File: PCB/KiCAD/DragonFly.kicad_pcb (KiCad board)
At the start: 2 copper layers, 120 x 93 mm, 136 parts, among them CON1 AVR-ISP-6, J1 USB_OTG, J2 JACK_TRS_3pins, J3 MIC, J7 Conn_Coaxial, K1 TQ2-12VDC, P4 CONN_01X01, P5 CONN_01X01, P6 CONN_01X01, P7 CONN_01X01, Q1 MMBFJ310LT1G, Q10 MMBT4401LT1G, Q11 BFG591, Q12 IRF610, Q2 MMBT2222A, Q3 SI2301-TP, Q4 SI2301-TP, Q5 MMBT2222A, Q6 MMBFJ310LT1G, T1 1_9, T2 1_4, T3 1_4, U1 ADE-1, U10 LD1117S33TR, U2 ATMEGA8-16AU, U3 ADuM1201CR, U4 LM78L06, U5 SA612, U6 FT232RL, U7 SI5351, U8 LM78L06, U9 SA612, Y1 8Mhz, Y2 8Mhz, Y3 8Mhz, Y4 8Mhz, Y5 8Mhz, Y6 8Mhz, Y7 8Mhz, Y8 27Mhz

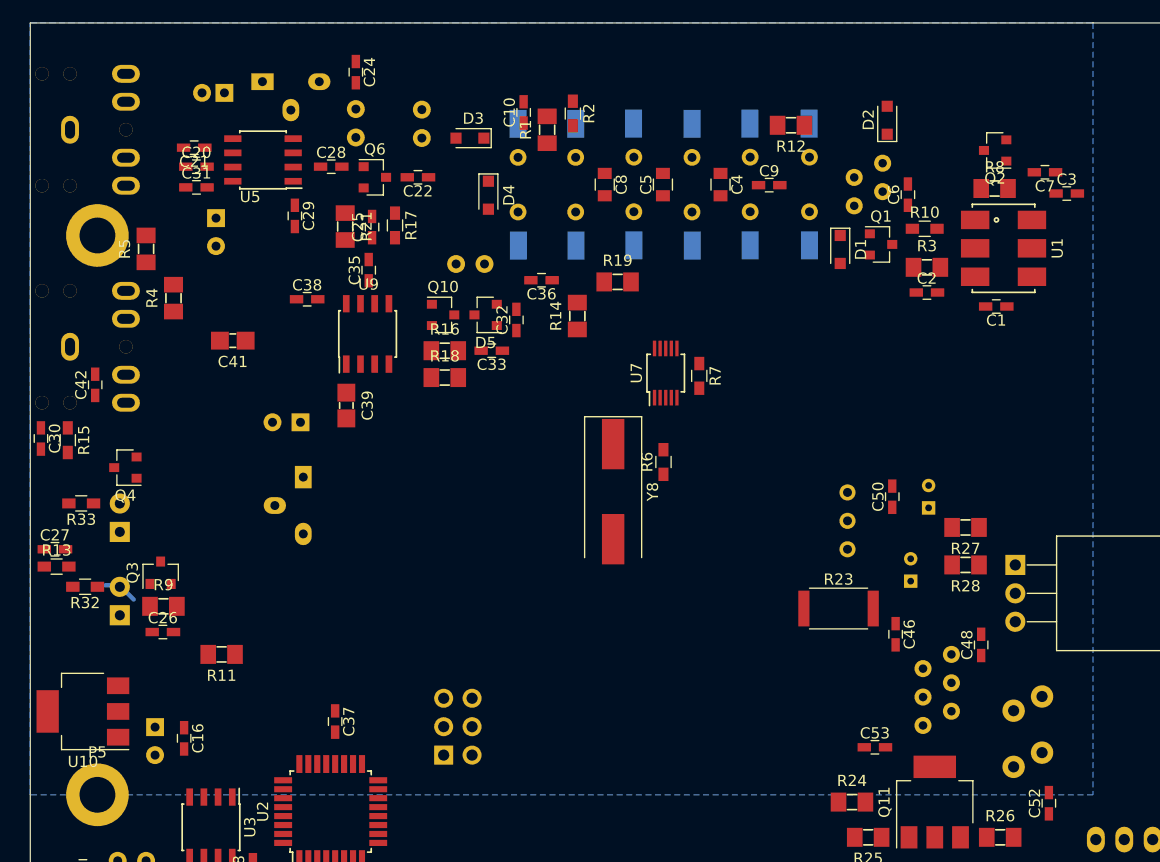
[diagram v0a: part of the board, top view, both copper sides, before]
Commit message: diode mixer on discrete components, begin move to DragonFly libs
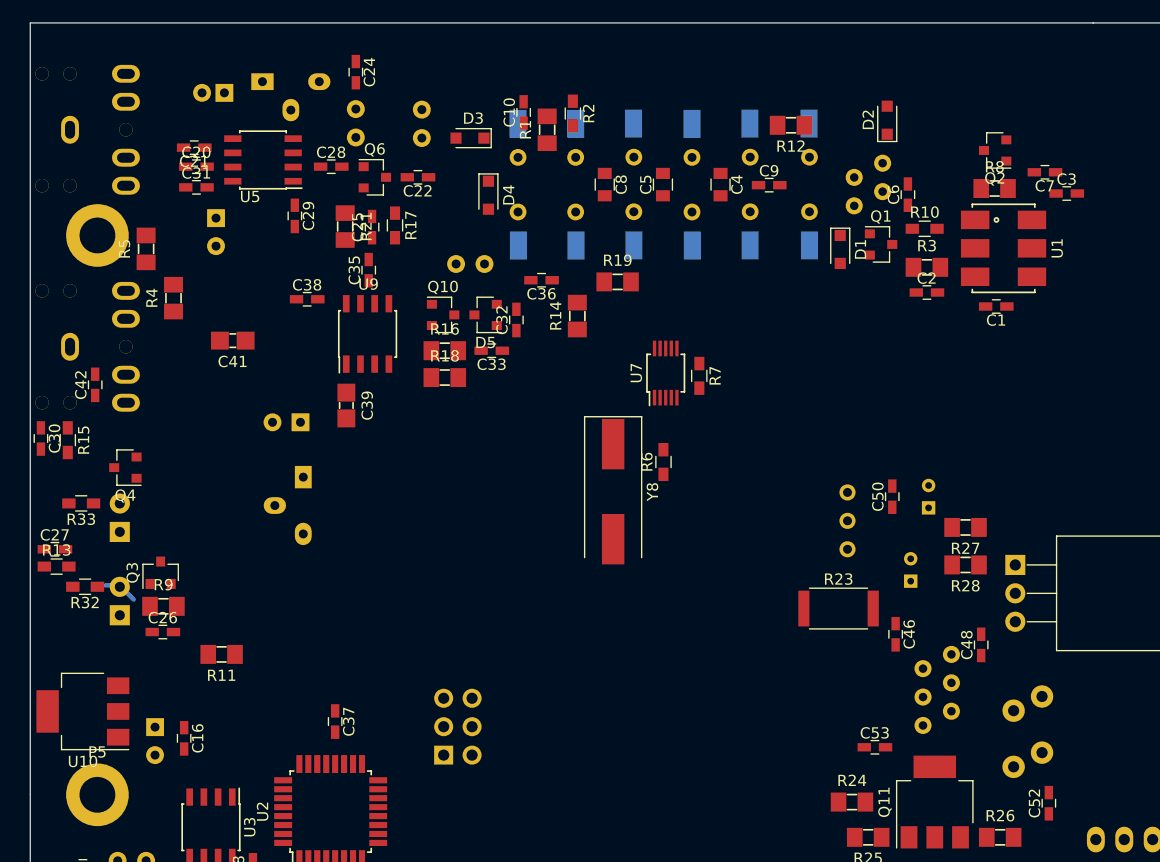
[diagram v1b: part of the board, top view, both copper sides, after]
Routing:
- removed copper zone on B.Cu, net GND
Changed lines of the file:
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@@
     (links 287)
     (no_connects 268)
-    (area 34.949999 19.949999 155.050001 113.050001)
+    (area 31.095 19.949999 157.085 176.075)
     (thickness 1.6)
     (drawings 6)
@@
   (layers
     (0 F.Cu signal)
-    (31 B.Cu signal hide)
+    (31 B.Cu signal)
     (32 B.Adhes user)
     (33 F.Adhes user)
@@
   (segment (start 41.7 70.27) (end 42.97 70.27) (width 0.4) (layer B.Cu) (net 88) (status 10))
   (segment (start 42.97 70.27) (end 44.24 71.54) (width 0.4) (layer B.Cu) (net 88) (status 20))
-  (zone (net 1) (net_name GND) (layer B.Cu) (hatch edge 0.508)
-    (connect_pads (clearance 0.2))
-    (min_thickness 0.2)
-    (fill yes (arc_segments 16) (thermal_gap 0.22) (thermal_bridge_width 0.501))
-    (polygon
-      (pts
-        (xy 130 89) (xy 35 89) (xy 35 20) (xy 130 20)
-      )
-    )
-  )
 )

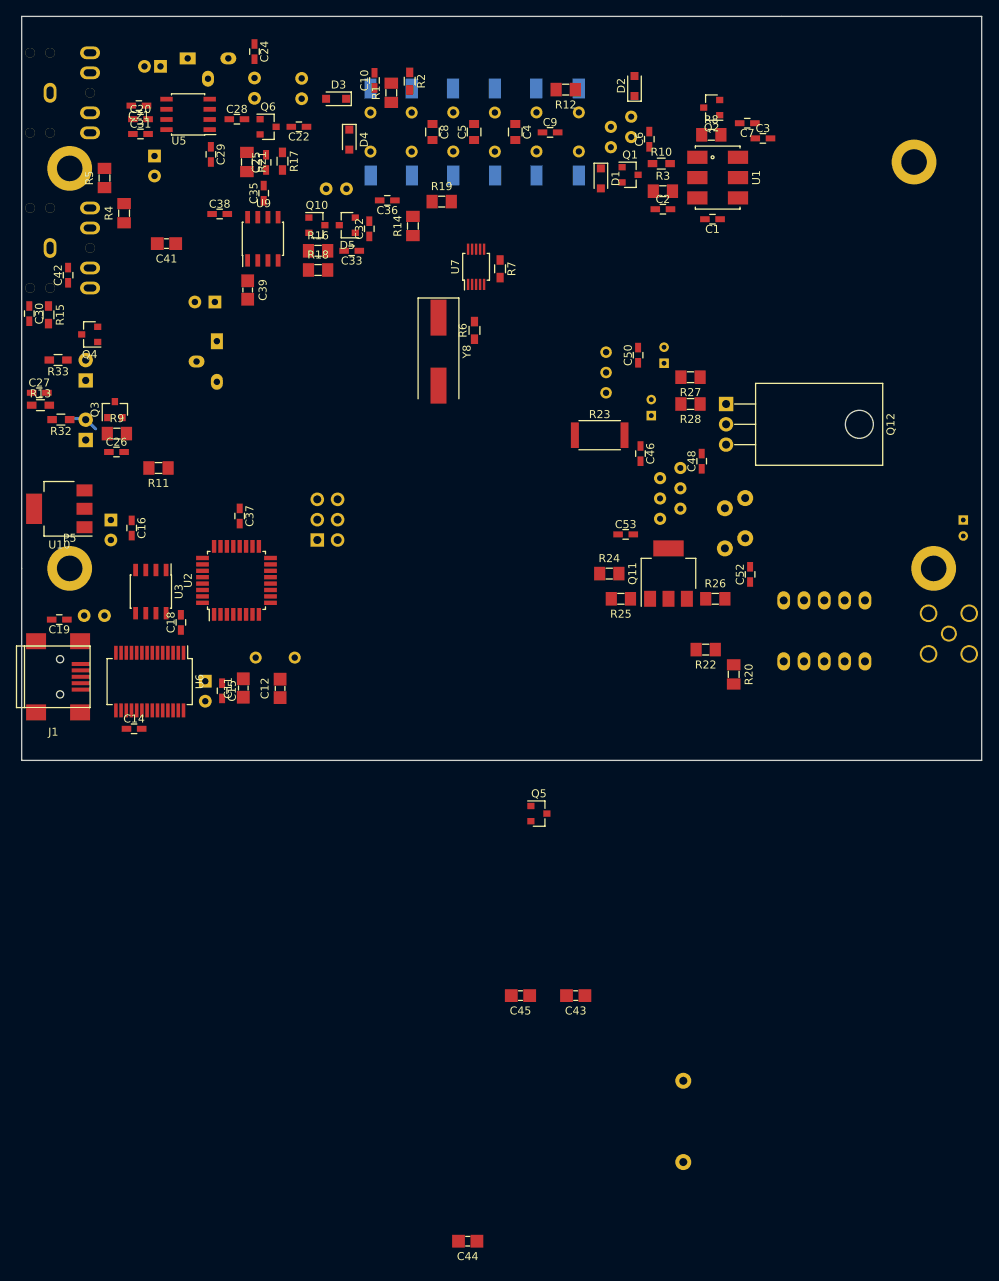
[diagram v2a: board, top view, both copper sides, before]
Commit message: PCB read works, layout BPF
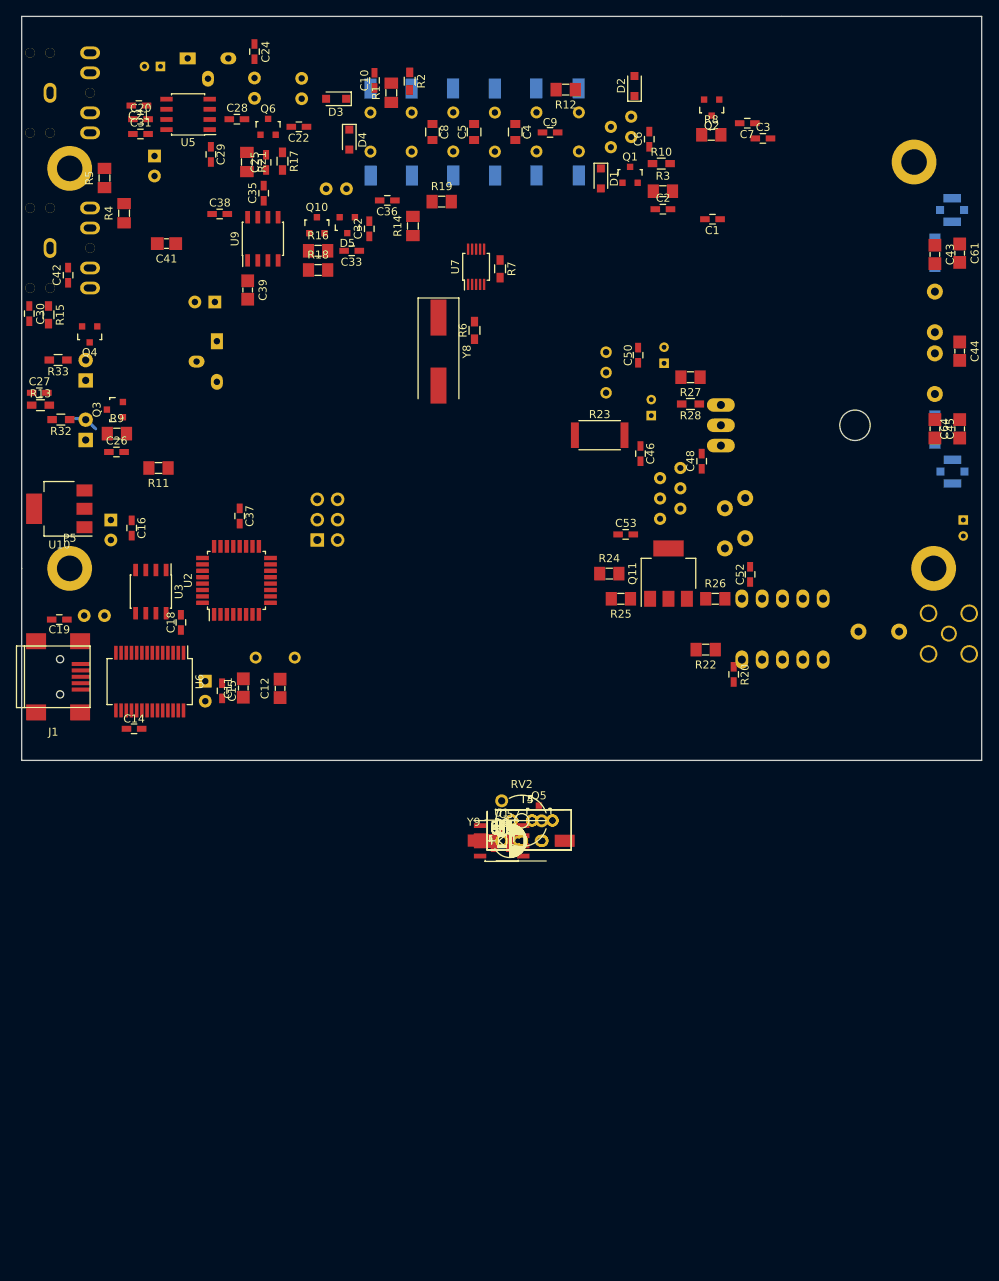
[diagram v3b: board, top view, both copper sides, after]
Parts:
- removed Q12: IRF610, TO_SOT_Packages_THT:TO-220-3_Horizontal
- added C54, C58: 100nF, Capacitors_SMD:C_0603_HandSoldering, F.Cu at (95.0, 123.1)
- added C55: 62, Capacitors_SMD:C_0805, F.Cu at (95.0, 123.1)
- added C56: 33nF, DragonFly:C_1206_0603, F.Cu at (95.0, 123.1)
- added C57: 10µF, DragonFly:CP_Radial_D4.0mm_P2.00mm, F.Cu at (95.0, 123.1)
- added C59: 4.7nF, DragonFly:C_0603_HandSoldering, F.Cu at (95.0, 123.1)
- added C60: 47nF, DragonFly:C_1206_0603, F.Cu at (95.0, 123.1)
- added C61: 560pF, DragonFly:C_1206_0603, F.Cu at (152.2, 49.6)
- added C62: C_Variable, Capacitors_SMD:C_Trimmer_Voltronics_JZ, B.Cu at (149.2, 49.5)
- added C63: C_Variable, Capacitors_SMD:C_Trimmer_Voltronics_JZ, B.Cu at (149.2, 71.7)
- added C64: 560pF, DragonFly:C_1206_0603, F.Cu at (152.2, 71.5)
- added C65: 10nF, DragonFly:C_0603_HandSoldering, F.Cu at (95.0, 123.1)
- added C66, C67: 560pF, DragonFly:C_1206_0603, F.Cu at (95.0, 123.1)
- added D11: LL4148, DragonFly:MiniMELF_Standard, F.Cu at (95.0, 123.1)
- added D8, D9: BAT54S, DragonFly:SOT-23, F.Cu at (95.0, 123.1)
- added J4: Conn_Coaxial, DragonFly:U.FL_Molex_MCRF_73412-0110_Vertical, B.Cu at (151.3, 44.2)
- added J5: Conn_Coaxial, DragonFly:U.FL_Molex_MCRF_73412-0110_Vertical, B.Cu at (151.3, 76.9)
- added L5: 1uH, DragonFly:Choke_Toroid_5x10mm_Vertical, B.Cu at (139.6, 102.0)
- added L7: 31uH, DragonFly:Choke_Toroid_5x10mm_Vertical, B.Cu at (144.1, 62.1)
- added Q7: IRF610, DragonFly:TO-220_Neutral123_Horizontal_LargePads, B.Cu at (122.4, 71.1)
- added R29, R30: 10K, DragonFly:R_1206_0603, F.Cu at (95.0, 123.1)
- added R31: 300R, DragonFly:R_1206_0603, F.Cu at (95.0, 123.1)
- added R34: 100k, DragonFly:R_1206_0603, F.Cu at (95.0, 123.1)
- added R35: 1k, DragonFly:R_0603_HandSoldering, F.Cu at (95.0, 123.1)
- added R36: 15k, DragonFly:R_0603_HandSoldering, F.Cu at (95.0, 123.1)
- added R37: 330, DragonFly:R_1206_0603, F.Cu at (95.0, 123.1)
- added R38: 3.3K, DragonFly:R_1206_0603, F.Cu at (95.0, 123.1)
- added RV2: 1k, Potentiometers:Potentiometer_Trimmer_Piher_PT-6v_Horizontal, F.Cu at (95.0, 123.1)
- added T4, T5: Transformer_1P_2S, DragonFly:HF12, F.Cu at (95.0, 123.1)
- added Y9: 8Mhz, DragonFly:Crystal_HC49-U_Vertical, F.Cu at (95.0, 123.1)
- C1, C2, C20, C24, C25, C26, C27, C28, C3, C30, C31, C32, C33, C35, C36, C38, C42, C48, C53, C6, C7: footprint Capacitors_SMD:C_0603_HandSoldering -> DragonFly:C_0603_HandSoldering
- C22: value 100nF -> 10nF; footprint Capacitors_SMD:C_0603_HandSoldering -> DragonFly:C_0603_HandSoldering
- C23: footprint Capacitors_THT:CP_Radial_D5.0mm_P2.00mm -> DragonFly:CP_Radial_D4.0mm_P2.00mm
- C34, C40: footprint Capacitors_THT:CP_Radial_D6.3mm_P2.50mm -> DragonFly:CP_Radial_D6.3mm_P2.50mm
- C44: value 390pF -> 1nF
- C47: footprint Capacitors_THT:CP_Radial_D4.0mm_P2.00mm -> DragonFly:CP_Radial_D4.0mm_P2.00mm
- D1, D2, D3, D4: footprint Diodes_SMD:D_SOD-323_HandSoldering -> DragonFly:D_SOD-323_HandSoldering
- D5, Q1, Q10, Q2, Q3, Q4, Q5, Q6: footprint TO_SOT_Packages_SMD:SOT-23 -> DragonFly:SOT-23
- D6, D7: footprint LEDs:LED_D3.0mm_Horizontal_O3.81mm_Z10.0mm -> DragonFly:LED_D3.0mm_Horizontal_O3.81mm_Z10.0mm
- J7: value Conn_Coaxial -> ANT; footprint Connectors:SMA_THT_Jack_Straight -> DragonFly:SMA_THT_Jack_Straight
- L6: value 52uH -> 31uH; footprint LCSDR:Resistor_Horizontal_RM10mm -> DragonFly:Choke_Toroid_5x10mm_Vertical
- Q11, U10: footprint TO_SOT_Packages_SMD:SOT-223 -> DragonFly:SOT-223
- R10, R13, R15, R17, R2, R32, R33: footprint Resistors_SMD:R_0603_HandSoldering -> DragonFly:R_0603_HandSoldering
- R20: footprint LCSDR:R_1206_0603 -> DragonFly:C_0603_HandSoldering
- R28: footprint LCSDR:R_1206_0603 -> DragonFly:R_0603_HandSoldering
- T1: footprint LCSDR:HF12 -> DragonFly:HF12
- U1: value ADE-1 -> NE5532; footprint DragonFly:ADE-1H -> DragonFly:SOIC-8_3.9x4.9mm_Pitch1.27mm
- U3, U5, U9: footprint Housings_SOIC:SOIC-8_3.9x4.9mm_Pitch1.27mm -> DragonFly:SOIC-8_3.9x4.9mm_Pitch1.27mm
- U4, U8: footprint TO_SOT_Packages_THT:TO-92_Molded_Wide_Oval -> DragonFly:TO-92_Molded_Wide_Oval
- moved C44 127.1 mm to (152.2, 61.9), turned to 270 degrees
- moved C43 103.0 mm to (149.2, 49.8), turned to 270 degrees
- moved L6 102.1 mm to (144.1, 54.4), turned to 0 degrees
- moved C45 87.8 mm to (149.2, 71.5), turned to 270 degrees
- moved U1 87.2 mm to (95.0, 123.1), turned to 0 degrees
- moved K1 5.23 mm to (125.0, 92.8)
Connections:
- C28 pad 2: Net-(C28-Pad2) -> GND
- C29 pad 2: GND -> Net-(C29-Pad2)
- C43 pad 1: Net-(C43-Pad1) -> BPF
- C44 pad 1: Net-(C43-Pad2) -> Net-(C44-Pad1)
- C45 pad 1: Net-(C43-Pad2) -> Net-(C45-Pad1)
- C45 pad 2: (no net) -> Net-(C45-Pad2)
- C53 pad 1: (no net) -> Net-(C53-Pad1)
- J1 pad 4: (no net) -> Net-(J1-Pad4)
- J2 pad 2: Net-(C23-Pad2) -> Net-(J2-Pad2)
- J2 pad 3: Net-(C23-Pad2) -> Net-(J2-Pad2)
- J2 pad 4: Net-(C23-Pad2) -> Net-(J2-Pad2)
- J2 pad 5: Net-(C23-Pad2) -> Net-(J2-Pad2)
- J7 pad 1: Net-(E1-Pad1) -> Net-(C67-Pad1)
- K1 pad 1: (no net) -> +12V
- K1 pad 10: (no net) -> Net-(D11-Pad2)
- K1 pad 3: Net-(E1-Pad1) -> Net-(C66-Pad1)
- K1 pad 5: (no net) -> Net-(K1-Pad5)
- K1 pad 6: (no net) -> Net-(K1-Pad6)
- K1 pad 8: (no net) -> Net-(C45-Pad2)
- L3 pad 2: Net-(C28-Pad2) -> Net-(C29-Pad2)
- L6 pad 1: BPF -> Net-(C43-Pad2)
- L6 pad 2: Net-(C43-Pad1) -> Net-(C44-Pad1)
- Q5 pad 1: (no net) -> Net-(C65-Pad1)
- Q5 pad 3: (no net) -> Net-(D11-Pad2)
- Q6 pad 1: Net-(C28-Pad2) -> Net-(C29-Pad2)
- U1 pad 1: Net-(Q2-Pad3) -> Net-(R34-Pad1)
- U1 pad 2: Net-(C1-Pad2) -> Net-(C57-Pad1)
- U1 pad 3: Net-(C2-Pad2) -> Net-(C56-Pad2)
- U1 pad 5: GND -> Net-(C59-Pad2)
- U1 pad 6: +12V -> Net-(C23-Pad1)
- U2 pad 1: (no net) -> Net-(U2-Pad1)
- U2 pad 10: (no net) -> Net-(U2-Pad10)
- U2 pad 11: (no net) -> Net-(U2-Pad11)
- U2 pad 12: (no net) -> Net-(U2-Pad12)
- U2 pad 13: (no net) -> Net-(U2-Pad13)
- U2 pad 14: (no net) -> Net-(U2-Pad14)
- U2 pad 19: (no net) -> Net-(U2-Pad19)
- U2 pad 2: (no net) -> Net-(U2-Pad2)
- U2 pad 22: (no net) -> Net-(U2-Pad22)
- U2 pad 23: (no net) -> Net-(U2-Pad23)
- U2 pad 25: (no net) -> Net-(U2-Pad25)
- U2 pad 26: (no net) -> Net-(U2-Pad26)
- U2 pad 32: (no net) -> Net-(U2-Pad32)
- U2 pad 9: (no net) -> Net-(U2-Pad9)
- U5 pad 4: (no net) -> Net-(C56-Pad2)
- U5 pad 5: Net-(C23-Pad1) -> Net-(U5-Pad5)
- U6 pad 10: (no net) -> Net-(U6-Pad10)
- U6 pad 11: (no net) -> Net-(U6-Pad11)
- U6 pad 12: (no net) -> Net-(U6-Pad12)
- U6 pad 13: (no net) -> Net-(U6-Pad13)
- U6 pad 14: (no net) -> Net-(U6-Pad14)
- U6 pad 2: (no net) -> Net-(U6-Pad2)
- U6 pad 22: (no net) -> Net-(U6-Pad22)
- U6 pad 23: (no net) -> Net-(U6-Pad23)
- U6 pad 27: (no net) -> Net-(U6-Pad27)
- U6 pad 28: (no net) -> Net-(U6-Pad28)
- U6 pad 3: (no net) -> Net-(U6-Pad3)
- U6 pad 6: (no net) -> Net-(U6-Pad6)
- U6 pad 9: (no net) -> Net-(U6-Pad9)
- U9 pad 4: (no net) -> Net-(U9-Pad4)
- Y4 pad 1: Net-(C5-Pad2) -> Net-(C55-Pad2)

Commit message: PCB progress, QER filter place, PA place
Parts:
- added C68: 62, Capacitors_SMD:C_0805, F.Cu at (122.4, 29.6)
- added Y10: 8Mhz, DragonFly:Crystal_HC49-U_Vertical, B.Cu at (119.5, 32.0)
- T4, T5, Y9: moved to B.Cu
- moved Y9 100.5 mm to (124.8, 27.1), turned to 270 degrees
- moved C55 96.5 mm to (118.0, 29.4), turned to 90 degrees
- moved T4 90.7 mm to (142.0, 45.4), turned to 180 degrees
- moved D9 86.3 mm to (140.4, 49.6), turned to 270 degrees
- moved D8 83.9 mm to (135.8, 49.8), turned to 90 degrees
- moved T5 79.3 mm to (133.4, 53.7)
- moved R30 57.8 mm to (145.8, 95.6), turned to 180 degrees
- moved R29 56.6 mm to (145.9, 98.3), turned to 180 degrees
- moved C66 52.3 mm to (141.0, 98.2)
- moved C67 50.6 mm to (142.8, 106.6), turned to 180 degrees
- moved C6 41.0 mm to (153.8, 28.2)
- moved Q1 40.9 mm to (151.3, 32.4), turned to 270 degrees
- moved T2 40.6 mm to (148.7, 29.3)
- moved D1 39.4 mm to (145.3, 29.8), turned to 180 degrees
- moved C9 37.8 mm to (138.5, 29.6)
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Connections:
- Q11 pad 2: Net-(Q11-Pad2) -> Net-(C53-Pad2)
- Q11 pad 4: Net-(C53-Pad2) -> Net-(Q11-Pad4)
- R22 pad 2: Net-(Q11-Pad2) -> Net-(C53-Pad2)
- R24 pad 2: Net-(Q11-Pad2) -> Net-(C53-Pad2)
- R31 pad 2: Net-(Q11-Pad2) -> Net-(Q11-Pad4)
- T1 pad 1: Net-(C53-Pad2) -> Net-(Q11-Pad4)
- Y9 pad 2: Net-(C55-Pad2) -> Net-(C68-Pad2)
